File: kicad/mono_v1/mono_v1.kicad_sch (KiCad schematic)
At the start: 69 parts, among them U1 RP2040_Zero

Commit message: Mono shape ok
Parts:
- D1, D10, D11, D12, D13, D14, D15, D16, D17, D18, D19, D2, D20, D21, D22, D23, D24, D25, D26, D27, D28, D29, D3, D30, D31, D32, D33, D34, D4, D5, D6, D7, D8, D9: footprint ScottoKeebs_Components:Diode_SOD-123_chew -> chew_is_so:Diode_SOD-123_chew; symbol ScottoKeebs:Placeholder_Diode -> chew_symbols:Placeholder_Diode
- S1, S10, S11, S12, S13, S15, S17, S18, S19, S2, S20, S21, S22, S23, S24, S25, S26, S27, S28, S29, S3, S30, S31, S32, S33, S34, S7, S8, S9: footprint ScottoKeebs_Choc:Choc_V1_chew -> chew_is_so:Choc_V1_chew; symbol ScottoKeebs:Placeholder_Keyswitch -> chew_symbols:Placeholder_Keyswitch
- S14, S16, S4, S5, S6: footprint ScottoKeebs_Choc:Choc_V1_chew -> chew_is_so:Choc_V1_chew_2; symbol ScottoKeebs:Placeholder_Keyswitch -> chew_symbols:Placeholder_Keyswitch
- U1: footprint ScottoKeebs_MCU:RP2040_Zero_chew_mono -> chew_is_so:RP2040_Zero_chew_mono; symbol ScottoKeebs:MCU_RP2040_Zero_chew_mono -> chew_symbols:MCU_RP2040_Zero_chew_mono
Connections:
- net Row 1: no longer D18.1 (K)
- net GND: now reaches U1.22 (GND)

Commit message: Mono prod
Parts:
- S17, S24: footprint chew_is_so:Choc_V1_chew -> chew_is_so:Choc_V1_chew_2
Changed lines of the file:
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@@
 			)
 		)
-		(property "Footprint" "chew_is_so:Choc_V1_chew"
+		(property "Footprint" "chew_is_so:Choc_V1_chew_2"
 			(at 127 92.71 0)
 			(effects
@@
 			)
 		)
-		(property "Footprint" "chew_is_so:Choc_V1_chew"
+		(property "Footprint" "chew_is_so:Choc_V1_chew_2"
 			(at 73.66 116.84 0)
 			(effects

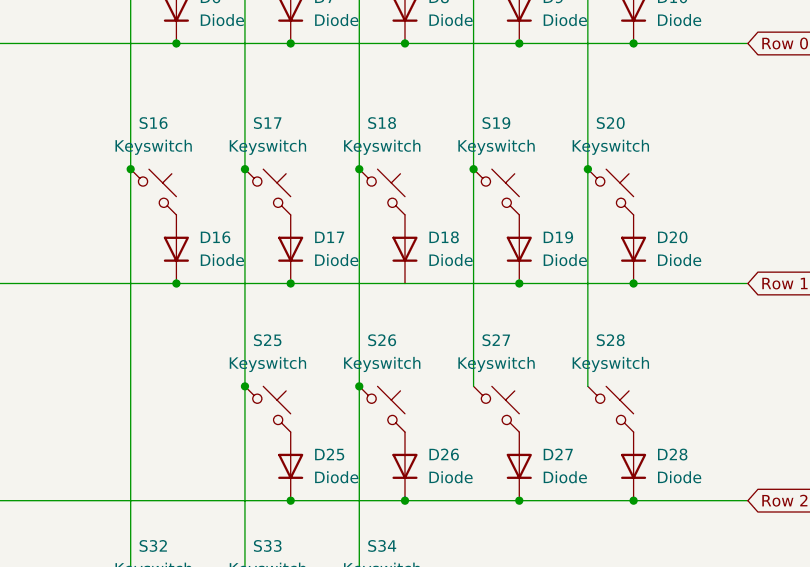
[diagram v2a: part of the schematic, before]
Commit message: Simplify switch traces
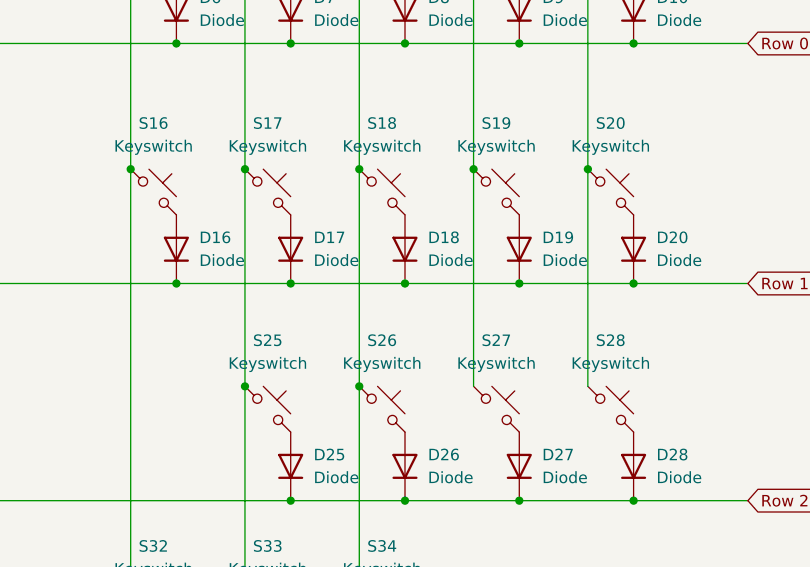
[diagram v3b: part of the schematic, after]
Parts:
- S14, S16, S17, S24, S4, S5, S6: footprint chew_is_so:Choc_V1_chew_2 -> chew_is_so:Choc_V1_chew
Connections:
- net Row 1: now also D18.1 (K)
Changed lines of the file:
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@@
 	)
 	(junction
+		(at 142.24 102.87)
+		(diameter 0)
+		(color 0 0 0 0)
+	)
+	(junction
 		(at 142.24 76.2)
 		(diameter 0)
@@
 	(wire
 		(pts
+			(xy 142.24 102.87) (xy 154.94 102.87)
+		)
+		(stroke
+			(width 0)
+			(type default)
+		)
+	)
+	(wire
+		(pts
 			(xy 50.8 102.87) (xy 63.5 102.87)
 		)
@@
 	(wire
 		(pts
-			(xy 129.54 102.87) (xy 154.94 102.87)
+			(xy 129.54 102.87) (xy 142.24 102.87)
 		)
 		(stroke
@@
 			)
 		)
-		(property "Footprint" "chew_is_so:Choc_V1_chew_2"
+		(property "Footprint" "chew_is_so:Choc_V1_chew"
 			(at 127 92.71 0)
 			(effects
@@
 			)
 		)
-		(property "Footprint" "chew_is_so:Choc_V1_chew_2"
+		(property "Footprint" "chew_is_so:Choc_V1_chew"
 			(at 73.66 66.04 0)
 			(effects
@@
 			)
 		)
-		(property "Footprint" "chew_is_so:Choc_V1_chew_2"
+		(property "Footprint" "chew_is_so:Choc_V1_chew"
 			(at 114.3 92.71 0)
 			(effects
@@
 			)
 		)
-		(property "Footprint" "chew_is_so:Choc_V1_chew_2"
+		(property "Footprint" "chew_is_so:Choc_V1_chew"
 			(at 73.66 116.84 0)
 			(effects
@@
 			)
 		)
-		(property "Footprint" "chew_is_so:Choc_V1_chew_2"
+		(property "Footprint" "chew_is_so:Choc_V1_chew"
 			(at 73.66 92.71 0)
 			(effects
@@
 			)
 		)
-		(property "Footprint" "chew_is_so:Choc_V1_chew_2"
+		(property "Footprint" "chew_is_so:Choc_V1_chew"
 			(at 114.3 66.04 0)
 			(effects
@@
 			)
 		)
-		(property "Footprint" "chew_is_so:Choc_V1_chew_2"
+		(property "Footprint" "chew_is_so:Choc_V1_chew"
 			(at 86.36 66.04 0)
 			(effects
